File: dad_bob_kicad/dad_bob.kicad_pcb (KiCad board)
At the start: 2 copper layers, 0 parts

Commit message: Added pcbNew files, block layouts complete
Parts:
- added C1: ECQ-UBAF474K, ECQ-UBAF4747K_kicad:ECQUBAF474K, F.Cu at (238.3, 85.6)
- added C10: 4pf, Capacitor_SMD:C_0805_2012Metric_Pad1.15x1.40mm_HandSolder, F.Cu at (174.7, 45.3)
- added C11: 4pf, Capacitor_SMD:C_0805_2012Metric_Pad1.15x1.40mm_HandSolder, F.Cu at (174.7, 47.9)
- added C12: 350pF, Capacitor_SMD:C_0805_2012Metric_Pad1.15x1.40mm_HandSolder, F.Cu at (188.1, 47.1)
- added C13: 350pF, Capacitor_SMD:C_0805_2012Metric_Pad1.15x1.40mm_HandSolder, F.Cu at (190.8, 47.1)
- added C14: CTRIM, Capacitor_SMD:C_Trimmer_Voltronics_JQ, F.Cu at (193.7, 47.1)
- added C15: 350pF, Capacitor_SMD:C_0805_2012Metric_Pad1.15x1.40mm_HandSolder, F.Cu at (188.1, 51.8)
- added C16: 350pF, Capacitor_SMD:C_0805_2012Metric_Pad1.15x1.40mm_HandSolder, F.Cu at (190.8, 52.0)
- added C17: CTRIM, Capacitor_SMD:C_Trimmer_Voltronics_JQ, F.Cu at (193.7, 51.9)
- added C18: 4pf, Capacitor_SMD:C_0805_2012Metric_Pad1.15x1.40mm_HandSolder, F.Cu at (174.7, 58.0)
- added C19: 4pf, Capacitor_SMD:C_0805_2012Metric_Pad1.15x1.40mm_HandSolder, F.Cu at (174.7, 55.5)
- added C2: 220pF, Capacitor_SMD:C_0805_2012Metric_Pad1.15x1.40mm_HandSolder, F.Cu at (266.4, 110.0)
- added C20: 4pf, Capacitor_SMD:C_0805_2012Metric_Pad1.15x1.40mm_HandSolder, F.Cu at (174.7, 53.1)
- added C21: 4pf, Capacitor_SMD:C_0805_2012Metric_Pad1.15x1.40mm_HandSolder, F.Cu at (174.7, 50.8)
- added C22: ~, Capacitor_SMD:C_0805_2012Metric_Pad1.15x1.40mm_HandSolder, F.Cu at (297.6, 143.5)
- added C23: 4pf, Capacitor_SMD:C_0805_2012Metric_Pad1.15x1.40mm_HandSolder, F.Cu at (239.5, 136.0)
- added C24: 4pf, Capacitor_SMD:C_0805_2012Metric_Pad1.15x1.40mm_HandSolder, F.Cu at (239.5, 138.6)
- added C25: 4pf, Capacitor_SMD:C_0805_2012Metric_Pad1.15x1.40mm_HandSolder, F.Cu at (239.5, 141.0)
- added C26: 4pf, Capacitor_SMD:C_0805_2012Metric_Pad1.15x1.40mm_HandSolder, F.Cu at (239.5, 143.4)
- added C27: ~, Capacitor_SMD:C_0805_2012Metric_Pad1.15x1.40mm_HandSolder, F.Cu at (297.5, 145.7)
- added C28: ~, Capacitor_SMD:C_0805_2012Metric_Pad1.15x1.40mm_HandSolder, F.Cu at (297.5, 141.3)
- added C29: 350pF, Capacitor_SMD:C_0805_2012Metric_Pad1.15x1.40mm_HandSolder, F.Cu at (254.0, 142.6)
- added C3: 86nF, Capacitor_SMD:C_0805_2012Metric_Pad1.15x1.40mm_HandSolder, F.Cu at (77.7, 138.9)
- added C30: 350pF, Capacitor_SMD:C_0805_2012Metric_Pad1.15x1.40mm_HandSolder, F.Cu at (256.4, 142.6)
- added C31: CTRIM, Capacitor_SMD:C_Trimmer_Voltronics_JQ, F.Cu at (259.4, 142.6)
- added C32: ~, Capacitor_SMD:C_0805_2012Metric_Pad1.15x1.40mm_HandSolder, F.Cu at (281.6, 138.1)
- added C33: 350pF, Capacitor_SMD:C_0805_2012Metric_Pad1.15x1.40mm_HandSolder, F.Cu at (254.0, 147.1)
- added C34: 350pF, Capacitor_SMD:C_0805_2012Metric_Pad1.15x1.40mm_HandSolder, F.Cu at (256.4, 147.1)
- added C35: CTRIM, Capacitor_SMD:C_Trimmer_Voltronics_JQ, F.Cu at (259.4, 147.1)
- added C36: ~, Capacitor_SMD:C_0805_2012Metric_Pad1.15x1.40mm_HandSolder, F.Cu at (287.3, 149.9)
- added C37: ~, Capacitor_SMD:C_0805_2012Metric_Pad1.15x1.40mm_HandSolder, F.Cu at (287.3, 152.1)
- added C38: 4pf, Capacitor_SMD:C_0805_2012Metric_Pad1.15x1.40mm_HandSolder, F.Cu at (239.5, 146.2)
- added C39: 4pf, Capacitor_SMD:C_0805_2012Metric_Pad1.15x1.40mm_HandSolder, F.Cu at (239.5, 148.6)
- added C4: 86nF, Capacitor_SMD:C_0805_2012Metric_Pad1.15x1.40mm_HandSolder, F.Cu at (121.7, 128.0)
- added C40: 4pf, Capacitor_SMD:C_0805_2012Metric_Pad1.15x1.40mm_HandSolder, F.Cu at (239.5, 151.0)
- added C41: 4pf, Capacitor_SMD:C_0805_2012Metric_Pad1.15x1.40mm_HandSolder, F.Cu at (239.5, 153.4)
- added C42: ~, Capacitor_SMD:C_0805_2012Metric_Pad1.15x1.40mm_HandSolder, F.Cu at (293.2, 143.3)
- added C43: ~, Capacitor_SMD:C_0805_2012Metric_Pad1.15x1.40mm_HandSolder, F.Cu at (280.8, 153.9)
- added C44: ~, Capacitor_SMD:C_0805_2012Metric_Pad1.15x1.40mm_HandSolder, F.Cu at (273.4, 147.1)
- added C45: ~, Capacitor_SMD:C_0805_2012Metric_Pad1.15x1.40mm_HandSolder, F.Cu at (273.4, 149.4)
- added C46: ~, Capacitor_SMD:C_0805_2012Metric_Pad1.15x1.40mm_HandSolder, F.Cu at (276.5, 146.1)
- added C47: ~, Capacitor_SMD:C_0805_2012Metric_Pad1.15x1.40mm_HandSolder, F.Cu at (273.4, 142.6)
- added C48: ~, Capacitor_SMD:C_0805_2012Metric_Pad1.15x1.40mm_HandSolder, F.Cu at (273.4, 144.8)
- added C49: ~, Capacitor_SMD:C_0805_2012Metric_Pad1.15x1.40mm_HandSolder, F.Cu at (307.1, 61.5)
- added C5: CP, Capacitor_SMD:C_Elec_5x5.4, F.Cu at (61.2, 39.6)
- added C50: ~, Capacitor_SMD:C_0805_2012Metric_Pad1.15x1.40mm_HandSolder, F.Cu at (296.7, 61.5)
- added C51: ~, Capacitor_SMD:C_0805_2012Metric_Pad1.15x1.40mm_HandSolder, F.Cu at (299.5, 61.5)
- added C52: ~, Capacitor_SMD:C_0805_2012Metric_Pad1.15x1.40mm_HandSolder, F.Cu at (302.0, 61.5)
- added C53: ~, Capacitor_SMD:C_0805_2012Metric_Pad1.15x1.40mm_HandSolder, F.Cu at (304.5, 61.5)
- added C54: ~, Capacitor_SMD:C_0805_2012Metric_Pad1.15x1.40mm_HandSolder, F.Cu at (318.5, 61.5)
- added C55: ~, Capacitor_SMD:C_0805_2012Metric_Pad1.15x1.40mm_HandSolder, F.Cu at (316.2, 61.5)
- added C56: ~, Capacitor_SMD:C_0805_2012Metric_Pad1.15x1.40mm_HandSolder, F.Cu at (320.8, 61.5)
- added C6: CP, Capacitor_SMD:C_Elec_5x5.4, F.Cu at (125.7, 48.3)
- added C7: 86nF, Capacitor_SMD:C_0805_2012Metric_Pad1.15x1.40mm_HandSolder, F.Cu at (167.6, 128.5)
- added C8: 4pf, Capacitor_SMD:C_0805_2012Metric_Pad1.15x1.40mm_HandSolder, F.Cu at (174.8, 40.3)
- added C9: 4pf, Capacitor_SMD:C_0805_2012Metric_Pad1.15x1.40mm_HandSolder, F.Cu at (174.8, 42.8)
- added D1: SMCJ9.0CA, SMCJ5:DIONM7959X262N, F.Cu at (266.4, 103.6)
- added D2: 1N4001, Diode_THT:D_DO-41_SOD81_P5.08mm_Vertical_AnodeUp, F.Cu at (66.9, 23.5)
- added D3: 1N4001, Diode_THT:D_DO-41_SOD81_P5.08mm_Vertical_AnodeUp, F.Cu at (130.9, 32.6)
- added D4: 1N4001, Diode_THT:D_DO-41_SOD81_P5.08mm_Vertical_AnodeUp, F.Cu at (62.5, 23.5)
- added D5: 1N4001, Diode_THT:D_DO-41_SOD81_P5.08mm_Vertical_AnodeUp, F.Cu at (126.6, 32.8)
- added FB1: Ferrite_Bead, Ferrite_THT:LairdTech_28C0236-0JW-10, F.Cu at (306.3, 54.9)
- added FB2: Ferrite_Bead, Ferrite_THT:LairdTech_28C0236-0JW-10, F.Cu at (321.1, 67.8)
- added FB3: Ferrite_Bead, Ferrite_THT:LairdTech_28C0236-0JW-10, F.Cu at (306.3, 67.8)
- added J1: Conn_01x01, kyuditsky_kicad_fp:Banana_Jack_S_RA_73099, F.Cu at (106.9, 136.9)
- added J10: Conn_01x03_Male, Connector_PinHeader_2.54mm:PinHeader_1x03_P2.54mm_Vertical, F.Cu at (157.7, 128.5)
- added J11: BNC5-J-P-GN-RA-BH2D, BNC5-J-P-GN-RA-BH2D_kicad:BNC5JPGNRABH2D, F.Cu at (70.1, 78.0)
- added J2: Conn_01x01, kyuditsky_kicad_fp:Banana_Jack_S_RA_73099, F.Cu at (121.7, 136.9)
- added J3: Conn_01x01, kyuditsky_kicad_fp:Banana_Jack_S_RA_73099, F.Cu at (152.9, 136.9)
- added J4: Conn_01x01, kyuditsky_kicad_fp:Banana_Jack_S_RA_73099, F.Cu at (167.6, 136.9)
- added J5: Conn_01x03_Male, Connector_PinHeader_2.54mm:PinHeader_1x03_P2.54mm_Vertical, F.Cu at (81.3, 137.7)
- added J6: Conn_02x15_Odd_Even, Connector_PinHeader_2.54mm:PinHeader_2x15_P2.54mm_Horizontal, F.Cu at (200.9, 88.6)
- added J7: BNC5-J-P-GN-RA-BH2D, BNC5-J-P-GN-RA-BH2D_kicad:BNC5JPGNRABH2D, F.Cu at (70.1, 135.1)
- added J8: Conn_01x03_Male, Connector_PinHeader_2.54mm:PinHeader_1x03_P2.54mm_Vertical, F.Cu at (111.8, 128.0)
- added J9: Conn_02x15_Odd_Even, Connector_PinSocket_2.54mm:PinSocket_2x15_P2.54mm_Horizontal, F.Cu at (189.5, 80.3)
- added K1: EC2-5NU, Relay_THT:Relay_DPDT_Kemet_EC2, F.Cu at (67.2, 27.7)
- added K2: EC2-5NU, Relay_THT:Relay_DPDT_Kemet_EC2, F.Cu at (131.2, 36.6)
- added Q1: 2N2219, Package_TO_SOT_THT:TO-39-3, F.Cu at (57.7, 31.0)
- added Q2: 2N2219, Package_TO_SOT_THT:TO-39-3, F.Cu at (121.7, 39.9)
- added Q3: AO3401A, Package_TO_SOT_SMD:SOT-23, F.Cu at (293.6, 61.5)
- added R1: 30M, Resistor_SMD:R_0805_2012Metric_Pad1.15x1.40mm_HandSolder, F.Cu at (77.7, 131.3)
- added R10: 50k, Resistor_SMD:R_0805_2012Metric_Pad1.15x1.40mm_HandSolder, F.Cu at (185.5, 47.1)
- added R11: DNP, Resistor_SMD:R_0805_2012Metric_Pad1.15x1.40mm_HandSolder, F.Cu at (196.6, 52.0)
- added R12: 50k, Resistor_SMD:R_0805_2012Metric_Pad1.15x1.40mm_HandSolder, F.Cu at (185.5, 51.8)
- added R13: 1M, Resistor_SMD:R_0805_2012Metric_Pad1.15x1.40mm_HandSolder, F.Cu at (179.4, 58.0)
- added R14: 1M, Resistor_SMD:R_0805_2012Metric_Pad1.15x1.40mm_HandSolder, F.Cu at (179.4, 55.5)
- added R15: 1M, Resistor_SMD:R_0805_2012Metric_Pad1.15x1.40mm_HandSolder, F.Cu at (179.5, 53.1)
- added R16: 1M, Resistor_SMD:R_0805_2012Metric_Pad1.15x1.40mm_HandSolder, F.Cu at (179.4, 50.8)
- added R17: ~, Resistor_SMD:R_0805_2012Metric_Pad1.15x1.40mm_HandSolder, F.Cu at (273.3, 140.3)
- added R18: ~, Resistor_SMD:R_0805_2012Metric_Pad1.15x1.40mm_HandSolder, F.Cu at (288.6, 140.4)
- added R19: 1M, Resistor_SMD:R_0805_2012Metric_Pad1.15x1.40mm_HandSolder, F.Cu at (244.2, 136.0)
- added R2: 30M, Resistor_SMD:R_0805_2012Metric_Pad1.15x1.40mm_HandSolder, F.Cu at (106.9, 128.0)
- added R20: 1M, Resistor_SMD:R_0805_2012Metric_Pad1.15x1.40mm_HandSolder, F.Cu at (244.2, 138.6)
- added R21: 1M, Resistor_SMD:R_0805_2012Metric_Pad1.15x1.40mm_HandSolder, F.Cu at (244.2, 141.0)
- added R22: 1M, Resistor_SMD:R_0805_2012Metric_Pad1.15x1.40mm_HandSolder, F.Cu at (244.2, 143.4)
- added R23: ~, Resistor_SMD:R_0805_2012Metric_Pad1.15x1.40mm_HandSolder, F.Cu at (281.6, 140.4)
- added R24: 50k, Resistor_SMD:R_0805_2012Metric_Pad1.15x1.40mm_HandSolder, F.Cu at (251.6, 142.6)
- added R25: DNP, Resistor_SMD:R_0805_2012Metric_Pad1.15x1.40mm_HandSolder, F.Cu at (262.3, 147.1)
- added R26: ~, Resistor_SMD:R_0805_2012Metric_Pad1.15x1.40mm_HandSolder, F.Cu at (284.4, 146.1)
- added R27: ~, Resistor_SMD:R_0805_2012Metric_Pad1.15x1.40mm_HandSolder, F.Cu at (288.7, 145.7)
- added R28: 50k, Resistor_SMD:R_0805_2012Metric_Pad1.15x1.40mm_HandSolder, F.Cu at (251.6, 147.1)
- added R29: ~, Resistor_SMD:R_0805_2012Metric_Pad1.15x1.40mm_HandSolder, F.Cu at (288.6, 138.2)
- added R3: 1k, Resistor_SMD:R_0805_2012Metric_Pad1.15x1.40mm_HandSolder, F.Cu at (56.1, 39.6)
- added R30: 1M, Resistor_SMD:R_0805_2012Metric_Pad1.15x1.40mm_HandSolder, F.Cu at (244.1, 146.2)
- added R31: 1M, Resistor_SMD:R_0805_2012Metric_Pad1.15x1.40mm_HandSolder, F.Cu at (244.1, 148.6)
- added R32: 1M, Resistor_SMD:R_0805_2012Metric_Pad1.15x1.40mm_HandSolder, F.Cu at (244.1, 151.0)
- added R33: 1M, Resistor_SMD:R_0805_2012Metric_Pad1.15x1.40mm_HandSolder, F.Cu at (244.1, 153.4)
- added R34: ~, Resistor_SMD:R_0805_2012Metric_Pad1.15x1.40mm_HandSolder, F.Cu at (293.2, 145.7)
- added R35: ~, Resistor_SMD:R_0805_2012Metric_Pad1.15x1.40mm_HandSolder, F.Cu at (273.3, 151.9)
- added R36: ~, Resistor_SMD:R_0805_2012Metric_Pad1.15x1.40mm_HandSolder, F.Cu at (293.2, 153.1)
- added R37: ~, Resistor_SMD:R_0805_2012Metric_Pad1.15x1.40mm_HandSolder, F.Cu at (280.8, 151.6)
- added R38: ~, Resistor_SMD:R_0805_2012Metric_Pad1.15x1.40mm_HandSolder, F.Cu at (309.6, 59.9)
- added R39: ~, Resistor_SMD:R_0805_2012Metric_Pad1.15x1.40mm_HandSolder, F.Cu at (309.6, 64.0)
- added R4: 1k, Resistor_SMD:R_0805_2012Metric_Pad1.15x1.40mm_HandSolder, F.Cu at (120.4, 48.3)
- added R5: 30M, Resistor_SMD:R_0805_2012Metric_Pad1.15x1.40mm_HandSolder, F.Cu at (152.9, 128.5)
- added R6: 1M, Resistor_SMD:R_0805_2012Metric_Pad1.15x1.40mm_HandSolder, F.Cu at (179.6, 40.3)
- added R7: 1M, Resistor_SMD:R_0805_2012Metric_Pad1.15x1.40mm_HandSolder, F.Cu at (179.6, 42.8)
- added R8: 1M, Resistor_SMD:R_0805_2012Metric_Pad1.15x1.40mm_HandSolder, F.Cu at (179.6, 45.3)
- added R9: 1M, Resistor_SMD:R_0805_2012Metric_Pad1.15x1.40mm_HandSolder, F.Cu at (179.6, 47.9)
- added RV1: VP4032K122R300, VP4032K122R300_kicad:CAPPM10080X500N, F.Cu at (259.8, 89.4)
- added T1: GT07-110-013, kyuditsky_kicad_fp:GT07110013, F.Cu at (254.8, 104.9)
- added U1: SL1002A600SP, kyuditsky_kicad_fp:SL1002A600SP, F.Cu at (251.0, 91.7)
- added U2: LTC6269, LTC6269:SOP65P490X110-9N, F.Cu at (280.9, 145.9)
- added U3: LTC6268, LTC6268IS6-10#TRMPBF:SOT95P280X100-6N, F.Cu at (293.3, 149.9)
- added U4: LTC6269, LTC6269:SOP65P490X110-9N, F.Cu at (313.2, 61.5)

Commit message: changed some layout, realized it needs some rework, but versioning for posterity
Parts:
- added D6: SMCJ5.0A, kyuditsky_kicad_fp:littlefuseTVS, F.Cu at (131.7, 146.3)
- added F1: 2.5a Fuse, Resistor_THT:R_Axial_DIN0204_L3.6mm_D1.6mm_P2.54mm_Vertical, F.Cu at (138.0, 149.3)
- added J12: USB4085-GF-A_REVA4, kyuditsky_kicad_fp:GCT_USB4085-GF-A_REVA4, F.Cu at (132.1, 158.4)
- added J13: Conn_01x03_Male, Connector_PinHeader_2.54mm:PinHeader_1x03_P2.54mm_Vertical, F.Cu at (105.2, 69.3)
- added J14: Conn_01x03_Male, Connector_PinHeader_2.54mm:PinHeader_1x03_P2.54mm_Vertical, F.Cu at (82.6, 147.2)
- added R40: 5.1k, Resistor_SMD:R_0805_2012Metric_Pad1.15x1.40mm_HandSolder, F.Cu at (128.8, 152.2)
- added R41: 5.1k, Resistor_SMD:R_0805_2012Metric_Pad1.15x1.40mm_HandSolder, F.Cu at (133.9, 152.2)
- C1: footprint ECQ-UBAF4747K_kicad:ECQUBAF474K -> ECQ-UBAF4747K_kicad:ECQ-UBAF474K-3_side
- C32, C42, C43: footprint Capacitor_SMD:C_0805_2012Metric_Pad1.15x1.40mm_HandSolder -> Capacitor_SMD:C_0603_1608Metric_Pad1.05x0.95mm_HandSolder
- D2, D3, D4, D5: footprint Diode_THT:D_DO-41_SOD81_P5.08mm_Vertical_AnodeUp -> Diode_THT:D_DO-41_SOD81_P2.54mm_Vertical_AnodeUp
- FB1, FB2, FB3: footprint Ferrite_THT:LairdTech_28C0236-0JW-10 -> Resistor_SMD:R_0603_1608Metric_Pad1.05x0.95mm_HandSolder
- Q1, Q2: value 2N2219 -> 2N3904; footprint Package_TO_SOT_THT:TO-39-3 -> Package_TO_SOT_THT:TO-92_Inline
- U2: footprint LTC6269:SOP65P490X110-9N -> kyuditsky_kicad_fp:SOP65P490X110-9N_LTC6269
- U3: footprint LTC6268IS6-10#TRMPBF:SOT95P280X100-6N -> kyuditsky_kicad_fp:SOT95P280X100-6N_LTC6268
- U4: value LTC6269 -> LM7301; footprint LTC6269:SOP65P490X110-9N -> kyuditsky_kicad_fp:SOIC127P600X175-8NLM7301
- moved FB2 214.1 mm to (110.0, 103.9), turned to 270 degrees
- moved FB1 211.0 mm to (102.5, 109.4), turned to 270 degrees
- moved FB3 190.3 mm to (119.4, 103.8), turned to 270 degrees
- moved C50 172.1 mm to (130.0, 104.3)
- moved C51 172.1 mm to (132.8, 104.3)
- moved Q3 172.1 mm to (126.9, 104.3)
- moved C49 172.1 mm to (140.4, 104.3)
- moved C53 172.1 mm to (137.9, 104.3)
- moved C52 172.1 mm to (135.3, 104.3)
- moved R38 172.1 mm to (142.9, 102.8)
- moved R39 172.1 mm to (142.9, 106.9)
- moved U4 171.5 mm to (147.2, 104.8), turned to 270 degrees
- moved C54 169.3 mm to (154.7, 104.3)
- moved C55 169.3 mm to (152.5, 104.3)
- moved C56 169.3 mm to (157.0, 104.3)
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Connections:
- C22 pad 1: GND -> GNDREF
- C28 pad 1: GND -> GNDREF
- C36 pad 1: GND -> GNDREF
- C37 pad 1: GND -> GNDREF
- C44 pad 2: GND -> GNDREF
- C45 pad 2: GND -> GNDREF
- C47 pad 2: GND -> GNDREF
- C48 pad 2: GND -> GNDREF
- C50 pad 1: V- -> GND
- C54 pad 2: GND -> GNDREF
- C55 pad 2: GND -> GNDREF
- C56 pad 2: GND -> GNDREF
- FB2 pad 1: GND -> GNDREF
- FB3 pad 2: V- -> GND
- J11 pad 2: GND -> GNDREF
- J11 pad 3: GND -> GNDREF
- J11 pad 4: GND -> GNDREF
- J11 pad 5: GND -> GNDREF
- Q3 pad 1: V- -> GND
- R25 pad 1: GND -> GNDREF
- R29 pad 1: GND -> GNDREF
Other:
- board text added: "!C32, C43, C42 all are all 0603!"

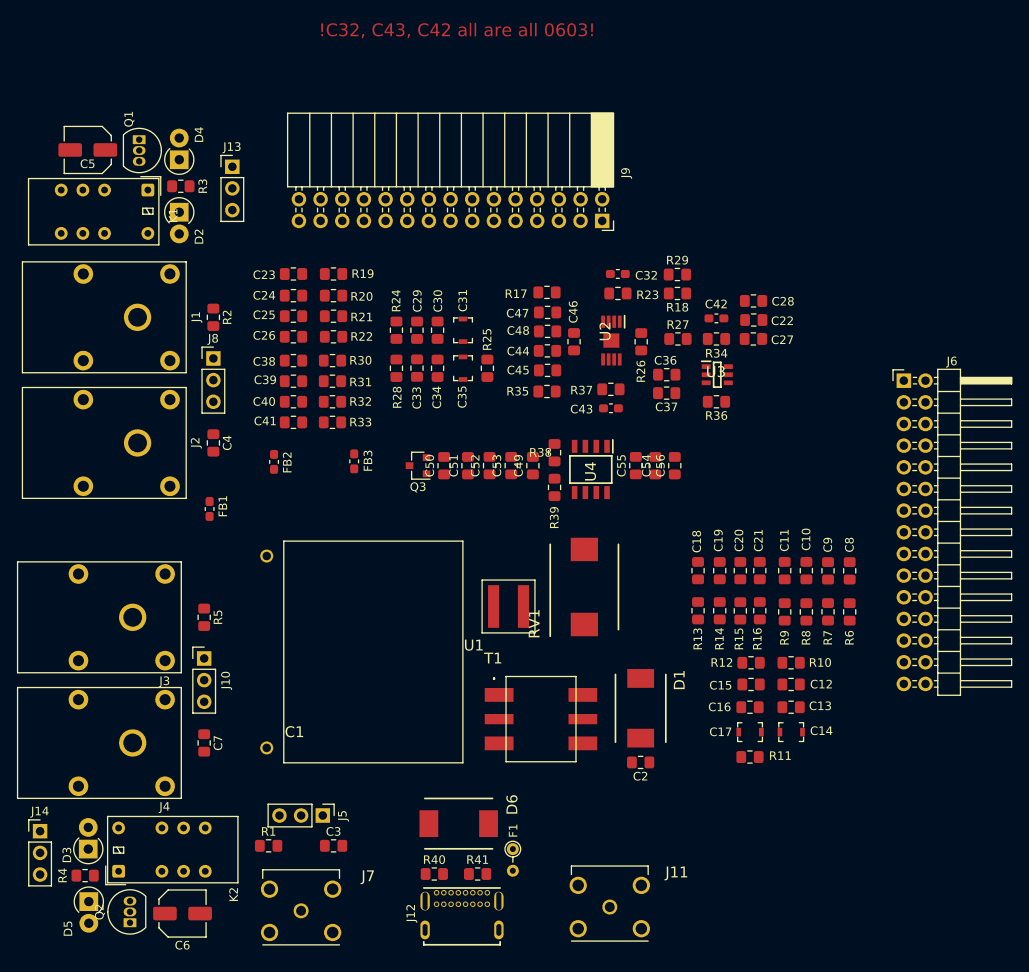
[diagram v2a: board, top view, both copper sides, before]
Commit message: End of day, layout reworked. Mostly ready to route
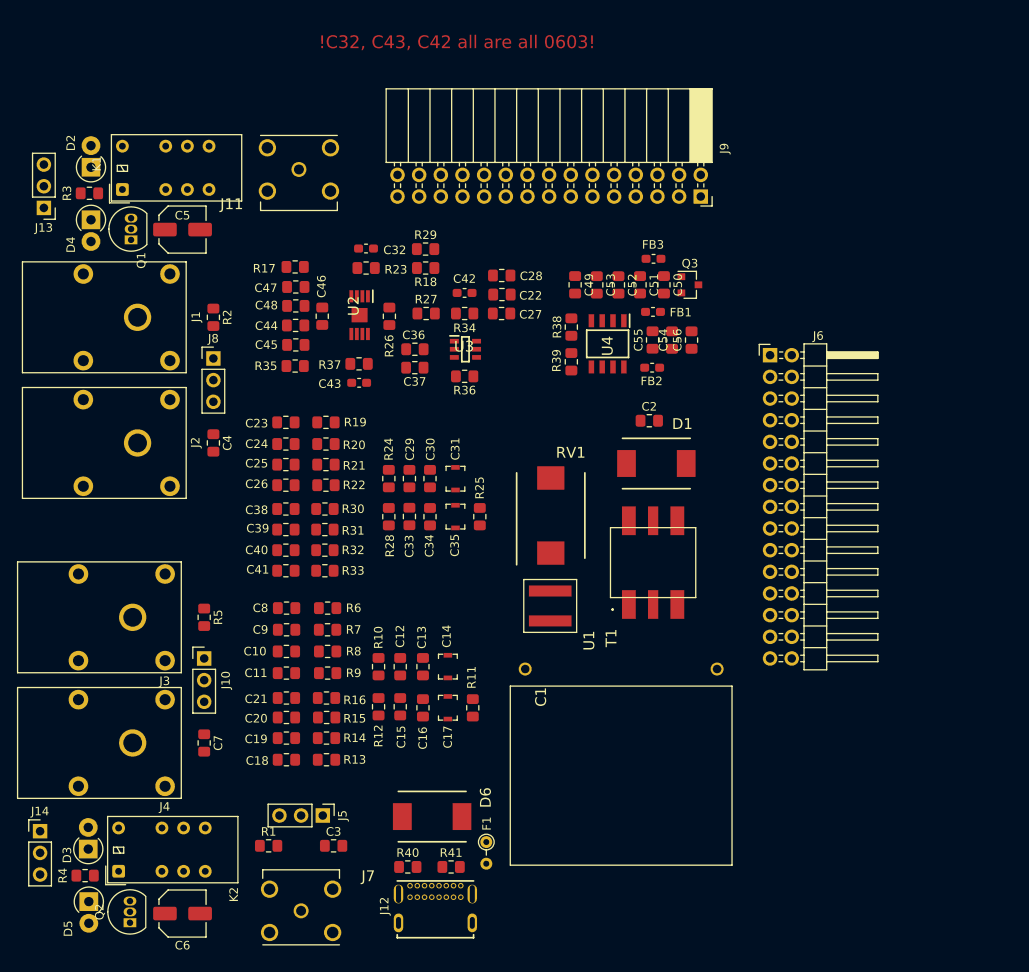
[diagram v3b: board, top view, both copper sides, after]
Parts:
- moved J11 93.9 mm to (113.0, 69.6), turned to 0 degrees
- moved C8 66.2 mm to (111.5, 121.0), turned to 0 degrees
- moved C9 63.9 mm to (111.5, 123.6), turned to 0 degrees
- moved C10 61.7 mm to (111.5, 126.1), turned to 0 degrees
- moved R6 61.2 mm to (116.3, 121.0), turned to 0 degrees
- moved C11 59.7 mm to (111.5, 128.7), turned to 0 degrees
- moved R7 58.7 mm to (116.3, 123.6), turned to 0 degrees
- moved C21 57.5 mm to (111.5, 131.6), turned to 0 degrees
- moved FB1 56.9 mm to (154.5, 86.3), turned to 0 degrees
- moved R8 56.3 mm to (116.3, 126.1), turned to 0 degrees
- moved C20 55.9 mm to (111.5, 133.9), turned to 0 degrees
- moved C19 54.5 mm to (111.5, 136.3), turned to 0 degrees
- moved R9 54.1 mm to (116.3, 128.7), turned to 0 degrees
- moved C18 53.1 mm to (111.5, 138.8), turned to 0 degrees
- moved R16 51.8 mm to (116.2, 131.6), turned to 0 degrees
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
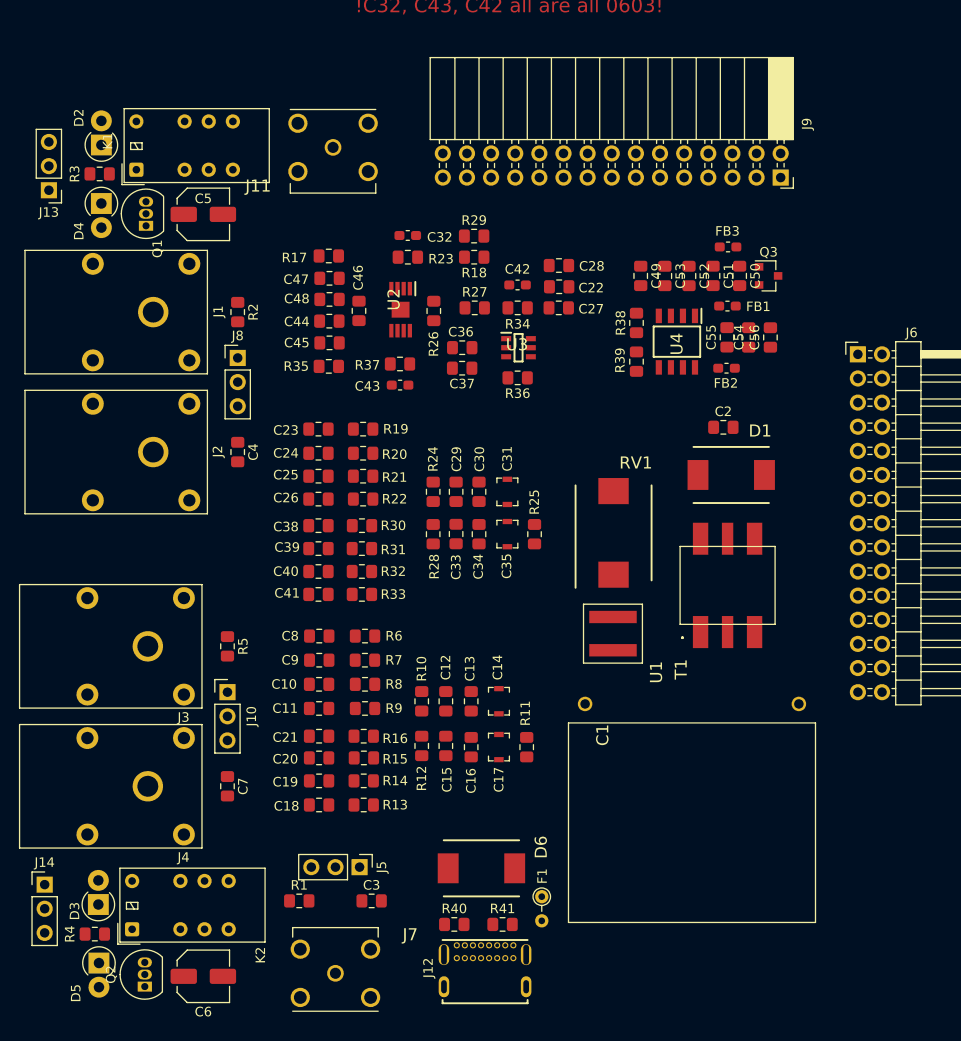
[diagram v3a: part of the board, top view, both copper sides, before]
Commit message: reworked layout
To begin routing
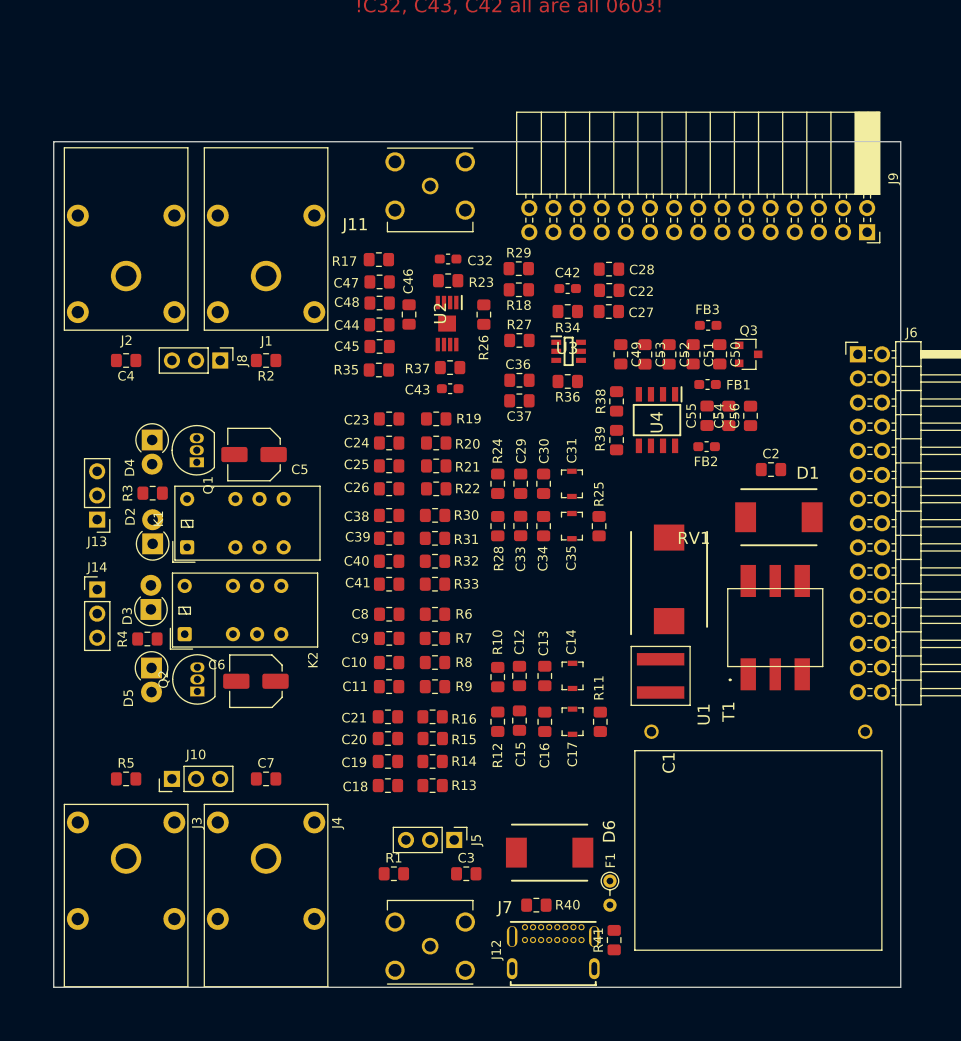
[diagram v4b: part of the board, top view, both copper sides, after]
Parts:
- moved D2 42.3 mm to (94.0, 111.3)
- moved K1 40.1 mm to (97.6, 111.7)
- moved J13 35.0 mm to (88.1, 108.8)
- moved R3 34.1 mm to (94.0, 106.0)
- moved J14 31.5 mm to (88.1, 116.1)
- moved C6 31.5 mm to (104.8, 125.8), turned to 180 degrees
- moved D3 31.5 mm to (93.8, 118.2)
- moved D5 31.5 mm to (93.9, 124.4)
- moved R4 31.5 mm to (93.4, 121.3)
- moved K2 31.5 mm to (97.4, 120.8)
- moved Q2 31.5 mm to (98.7, 126.9)
- moved C5 25.8 mm to (104.6, 101.9), turned to 180 degrees
- moved D4 25.5 mm to (93.9, 100.4)
- moved Q1 25.5 mm to (98.6, 102.7)
- moved J3 22.5 mm to (91.2, 144.4), turned to -90 degrees
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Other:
- board outline added: 89.2 x 89 mm
- net class Default removed
